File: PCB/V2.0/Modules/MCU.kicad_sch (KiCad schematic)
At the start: 4 parts, among them J13 Conn_02x04_Odd_Even, J15 Conn_02x04_Odd_Even, J28 Conn_02x20, J4 Conn_01x20

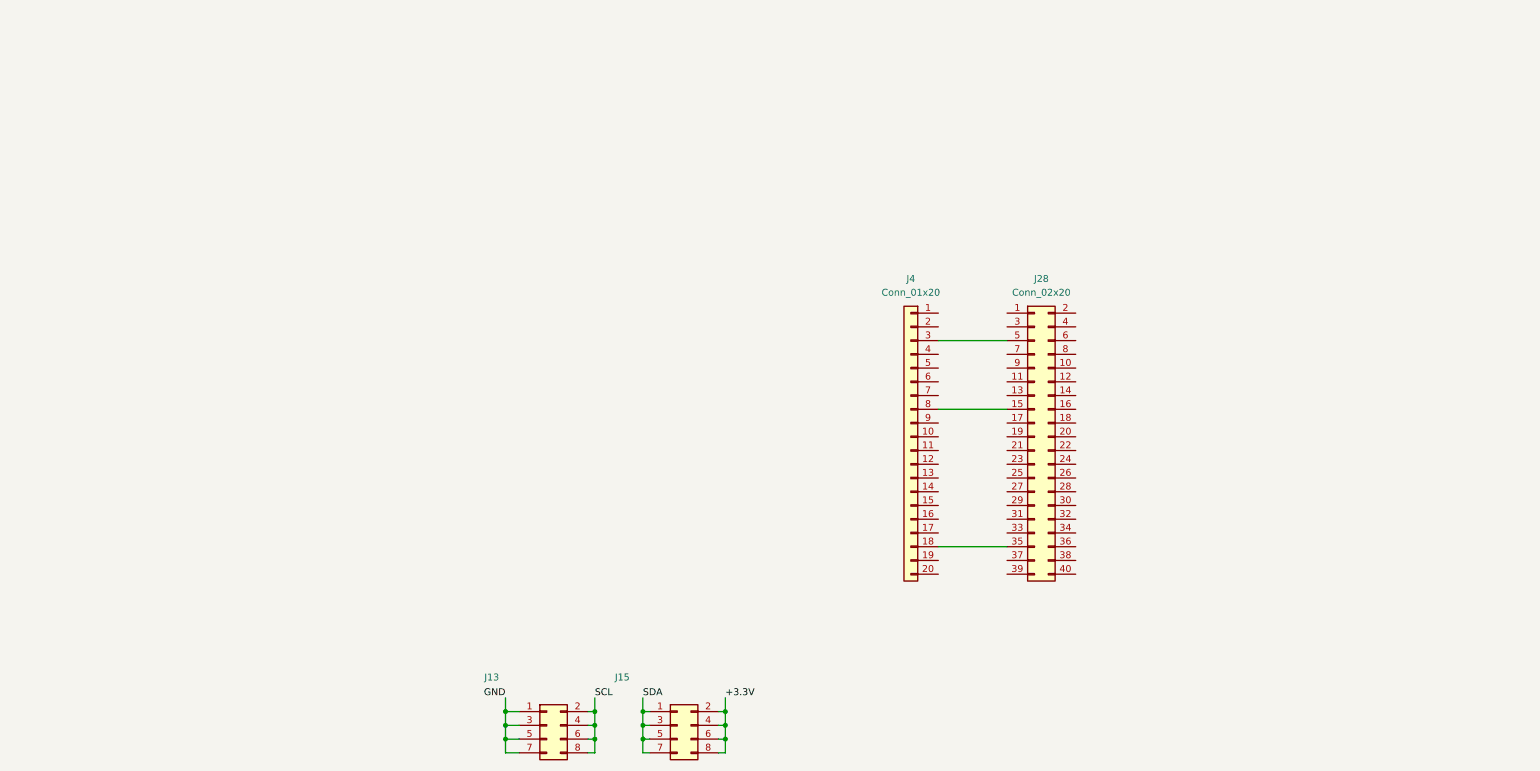
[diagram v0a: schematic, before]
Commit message: Update 2.0 - IMU and NRF24 support
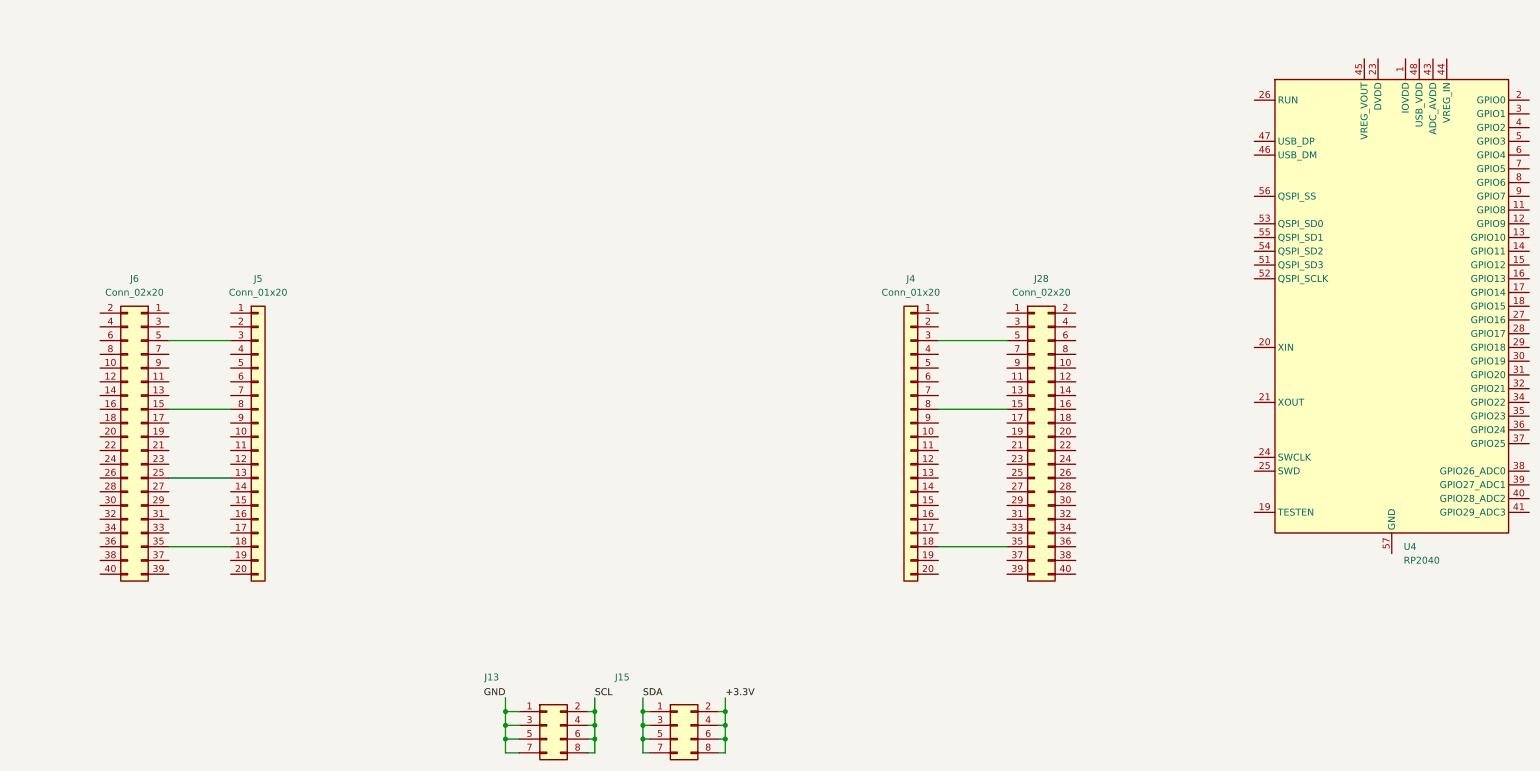
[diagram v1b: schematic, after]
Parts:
- added J5: Conn_01x20, Connector_PinSocket_2.54mm:PinSocket_1x20_P2.54mm_Vertical, symbol Connector_Generic:Conn_01x20
- added J6: Conn_02x20, Connector_PinHeader_2.54mm:PinHeader_2x20_P2.54mm_Vertical, symbol Connector_Generic:Conn_02x20_Odd_Even
- added U4: RP2040, Package_DFN_QFN:QFN-56-1EP_7x7mm_P0.4mm_EP3.2x3.2mm, symbol MCU_RaspberryPi:RP2040
- J4: footprint Connector_PinSocket_2.54mm:PinSocket_2x10_P2.54mm_Vertical -> Connector_PinSocket_2.54mm:PinSocket_1x20_P2.54mm_Vertical
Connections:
- new net: J5.13 (Pin_13), J6.25 (Pin_25)
- new net: J5.18 (Pin_18), J6.35 (Pin_35)
- new net: J5.3 (Pin_3), J6.5 (Pin_5)
- new net: J5.8 (Pin_8), J6.15 (Pin_15)
- new net: U4.1 (IOVDD), U4.10 (IOVDD), U4.22 (IOVDD), U4.33 (IOVDD), U4.42 (IOVDD), U4.49 (IOVDD)
- new net: U4.23 (DVDD), U4.50 (DVDD)

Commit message: Update V2.0 form factor
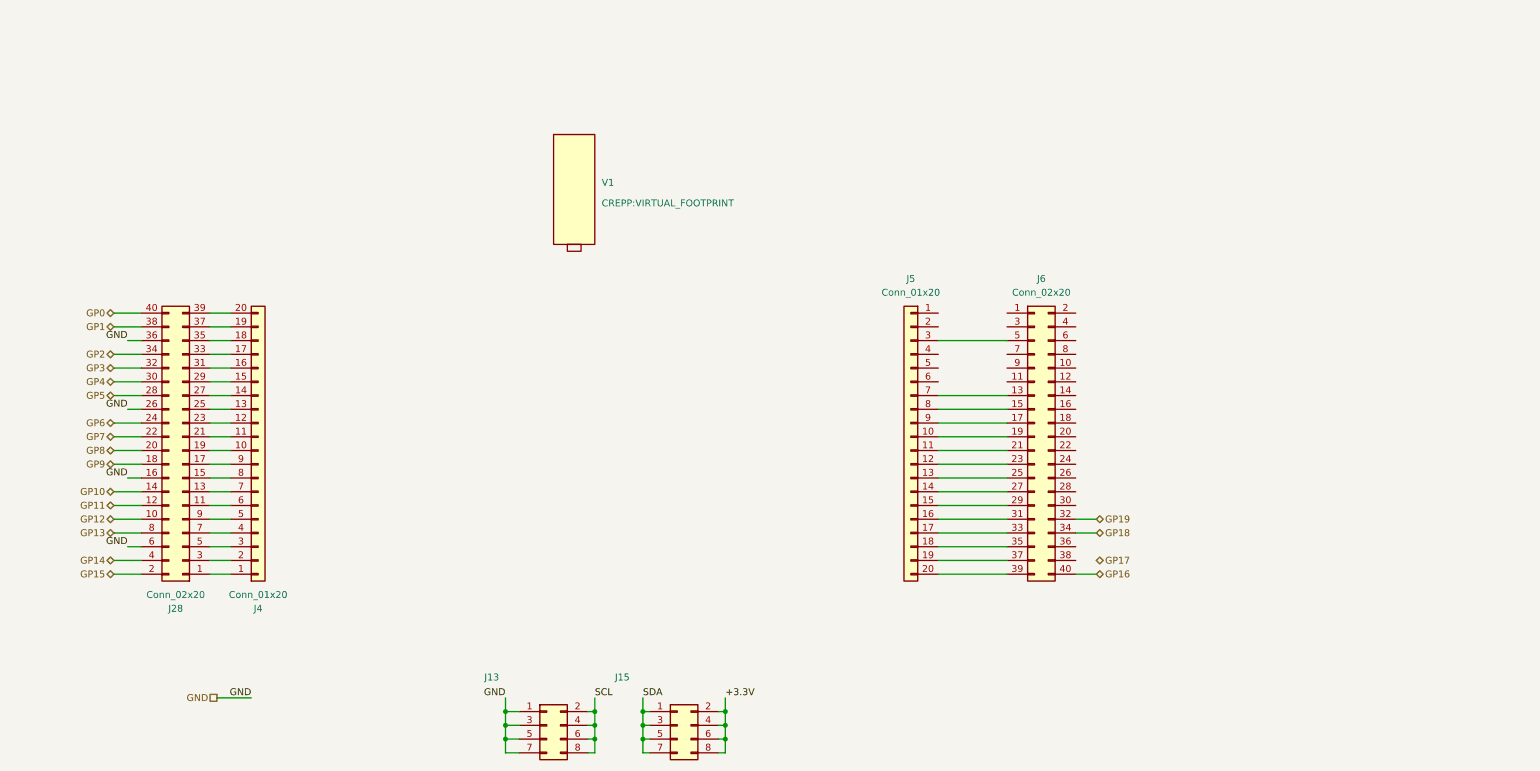
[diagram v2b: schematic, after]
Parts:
- removed U4: RP2040, Package_DFN_QFN:QFN-56-1EP_7x7mm_P0.4mm_EP3.2x3.2mm, symbol MCU_RaspberryPi:RP2040
- added V1: ~, CREPP:VIRTUAL_FOOTPRINT, symbol CREPP:RPI_PICO_VIRTUAL
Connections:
- net GND: now also J28.16 (Pin_16), J28.26 (Pin_26), J28.36 (Pin_36), J28.6 (Pin_6)
- net at J5.10 (Pin_10): now also J6.19 (Pin_19)
- net at J5.11 (Pin_11): now also J6.21 (Pin_21)
- net at J5.12 (Pin_12): now also J6.23 (Pin_23)
- net at J5.14 (Pin_14): now also J6.27 (Pin_27)
- net at J5.15 (Pin_15): now also J6.29 (Pin_29)
- net at J5.16 (Pin_16): now also J6.31 (Pin_31)
- net at J5.17 (Pin_17): now also J6.33 (Pin_33)
- net at J5.19 (Pin_19): now also J6.37 (Pin_37)
- net at J5.20 (Pin_20): now also J6.39 (Pin_39)
- net at J5.7 (Pin_7): now also J6.13 (Pin_13)
- net at J5.9 (Pin_9): now also J6.17 (Pin_17)
- net at J4.1 (Pin_1): now also J28.1 (Pin_1)
- net at J4.10 (Pin_10): now also J28.19 (Pin_19)
- net at J4.11 (Pin_11): now also J28.21 (Pin_21)
- net at J4.12 (Pin_12): now also J28.23 (Pin_23)
- net at J4.13 (Pin_13): now also J28.25 (Pin_25)
- net at J4.14 (Pin_14): now also J28.27 (Pin_27)
- net at J4.15 (Pin_15): now also J28.29 (Pin_29)
- net at J4.16 (Pin_16): now also J28.31 (Pin_31)
- net at J4.17 (Pin_17): now also J28.33 (Pin_33)
- net at J4.19 (Pin_19): now also J28.37 (Pin_37)
- net at J4.2 (Pin_2): now also J28.3 (Pin_3)
- net at J4.20 (Pin_20): now also J28.39 (Pin_39)
- net at J4.4 (Pin_4): now also J28.7 (Pin_7)
- net at J4.5 (Pin_5): now also J28.9 (Pin_9)
- net at J4.6 (Pin_6): now also J28.11 (Pin_11)
- net at J4.7 (Pin_7): now also J28.13 (Pin_13)
- net at J4.9 (Pin_9): now also J28.17 (Pin_17)
- net GP12: now reaches J28.10 (Pin_10)
- net GP11: now reaches J28.12 (Pin_12)
- net GP10: now reaches J28.14 (Pin_14)
- net GP9: now reaches J28.18 (Pin_18)
- net GP15: now reaches J28.2 (Pin_2)
- net GP8: now reaches J28.20 (Pin_20)
- net GP7: now reaches J28.22 (Pin_22)
- net GP6: now reaches J28.24 (Pin_24)
- net GP5: now reaches J28.28 (Pin_28)
- net GP4: now reaches J28.30 (Pin_30)
- net GP3: now reaches J28.32 (Pin_32)
- net GP2: now reaches J28.34 (Pin_34)
- net GP1: now reaches J28.38 (Pin_38)
- net GP14: now reaches J28.4 (Pin_4)
- net GP0: now reaches J28.40 (Pin_40)
- net GP13: now reaches J28.8 (Pin_8)
- net GP19: now reaches J6.32 (Pin_32)
- net GP18: now reaches J6.34 (Pin_34)
- net GP16: now reaches J6.40 (Pin_40)
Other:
- moved on the sheet: J28, J4, J5, J6

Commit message: Add img
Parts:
- added JP1, JP2, JP3: Jumper_2.54mm_red, CREPP_Jumpers:Jumper_2.54mm_red, symbol CREPP_Jumpers:Jumper_2.54mm_red
- added JP10, JP11, JP12, JP13, JP14, JP15, JP16, JP17, JP18, JP19, JP20, JP21, JP22, JP23, JP24, JP25, JP26, JP27, JP28, JP29, JP4, JP5, JP6, JP7, JP8, JP9: Jumper_2.54mm_green, CREPP_Jumpers:Jumper_2.54mm_green, symbol CREPP_Jumpers:Jumper_2.54mm_green
- added SERVO_SG1: ~, CREPP_Servo:SG90_Servo, symbol CREPP_Servomotors:Servomotor_SG90

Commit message: Update board
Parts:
- added SW9: SW_Left, Button_Switch_THT:SW_PUSH_6mm, symbol Switch:SW_Push
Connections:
- net GP4 is gone; now on net SDA: J28.30 (Pin_30)
- net GP5 is gone; now on net SCL: J28.28 (Pin_28)
- net +3.3V: now also J6.10 (Pin_10)
- net GND: now also J6.16 (Pin_16), J6.26 (Pin_26), J6.6 (Pin_6), SW9.2
- net at J5.1 (Pin_1): now also J6.1 (Pin_1)
- net RUN: now reaches J5.11 (Pin_11), J6.21 (Pin_21)
- net RUN: now also J6.22 (Pin_22), SW9.1
- net at J5.2 (Pin_2): now also J6.3 (Pin_3)
- net at J5.4 (Pin_4): now also J6.7 (Pin_7)
- net at J5.5 (Pin_5): now also J6.9 (Pin_9)
- net at J5.6 (Pin_6): now also J6.11 (Pin_11)
- net V_{BUS}: now reaches J6.2 (Pin_2)
- net GP22: now reaches J6.24 (Pin_24)
- net GP21: now reaches J6.28 (Pin_28)
- net GP20: now reaches J6.30 (Pin_30)
- net V_{SYS}: now reaches J6.4 (Pin_4)
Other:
- moved on the sheet: J13, J15, J28, J4, J5, J6, JP1, JP10, JP11, JP12, JP13, JP14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

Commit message: Update
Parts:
- removed JP8, JP9: Jumper_2.54mm_green, CREPP_Jumpers:Jumper_2.54mm_green, symbol CREPP_Jumpers:Jumper_2.54mm_green
- added JP8, JP9: Jumper_2.54mm_blue, CREPP_Jumpers:Jumper_2.54mm_blue, symbol CREPP_Jumpers:Jumper_2.54mm_blue
- SW9: value SW_Left -> SW_Reset
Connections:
- net GND: now also J6.36 (Pin_36)
- net GP17: now also J6.38 (Pin_38)
- net GP26: now also J6.20 (Pin_20)
- net GP27: now also J6.18 (Pin_18)
- net GP28: now also J6.14 (Pin_14)
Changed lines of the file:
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@@
 	(wire
 		(pts
+			(xy 247.65 118.11) (xy 251.46 118.11)
+		)
+		(stroke
+			(width 0)
+			(type default)
+		)
+	)
+	(wire
+		(pts
 			(xy 167.64 151.13) (xy 167.64 153.67)
 		)
@@
 	(wire
 		(pts
+			(xy 247.65 87.63) (xy 251.46 87.63)
+		)
+		(stroke
+			(width 0)
+			(type default)
+		)
+	)
+	(wire
+		(pts
 			(xy 87.63 105.41) (xy 91.44 105.41)
 		)
@@
 	(wire
 		(pts
+			(xy 247.65 115.57) (xy 251.46 115.57)
+		)
+		(stroke
+			(width 0)
+			(type default)
+		)
+	)
+	(wire
+		(pts
 			(xy 222.25 82.55) (xy 234.95 82.55)
 		)
@@
 	(wire
 		(pts
+			(xy 247.65 92.71) (xy 251.46 92.71)
+		)
+		(stroke
+			(width 0)
+			(type default)
+		)
+	)
+	(wire
+		(pts
 			(xy 247.65 113.03) (xy 251.46 113.03)
 		)
@@
 	(wire
 		(pts
+			(xy 247.65 95.25) (xy 251.46 95.25)
+		)
+		(stroke
+			(width 0)
+			(type default)
+		)
+	)
+	(wire
+		(pts
 			(xy 69.85 95.25) (xy 74.93 95.25)
 		)
@@
 	)
 	(label "GND"
+		(at 251.46 115.57 0)
+		(effects
+			(font
+				(size 1.27 1.27)
+			)
+			(justify left bottom)
+		)
+	)
+	(label "GND"
 		(at 251.46 77.47 0)
 		(effects
@@
 	(symbol
 		(lib_id "CREPP_Jumpers:Jumper_2.54mm_green")
-		(at 24.13 87.63 0)
-		(unit 1)
-		(exclude_from_sim yes)
-		(in_bom yes)
-		(on_board yes)
-		(dnp no)
-		(fields_autoplaced yes)
-		(property "Reference" "JP9"
-			(at 27.94 86.9949 0)
-			(effects
-				(font
-					(size 1.27 1.27)
-				)
-				(justify left)
-			)
-		)
-		(property "Value" "Jumper_2.54mm_green"
-			(at 24.13 89.916 0)
-			(effects
-				(font
-					(size 1.27 1.27)
-				)
-				(hide yes)
-			)
-		)
-		(property "Footprint" "CREPP_Jumpers:Jumper_2.54mm_green"
-			(at 24.13 87.63 0)
-			(effects
-				(font
-					(size 1.27 1.27)
-				)
-				(hide yes)
-			)
-		)
-		(property "Datasheet" "~"
-			(at 24.13 87.63 0)
-			(effects
-				(font
-					(size 1.27 1.27)
-				)
-				(hide yes)
-			)
-		)
-		(property "Description" "Jumper, 2-pole, open"
-			(at 24.13 87.63 0)
-			(effects
-				(font
-					(size 1.27 1.27)
-				)
-				(hide yes)
-			)
-		)
-		(instances
-			(project "CREPP.io"
-				(path "/8bcd0d00-b75f-4070-8d50-196a2022a31c/e5758719-e9ac-47cc-b357-8148e1c54986"
-					(reference "JP9")
-					(unit 1)
-				)
-			)
-		)
-	)
-	(symbol
-		(lib_id "CREPP_Jumpers:Jumper_2.54mm_green")
 		(at 262.89 113.03 0)
 		(unit 1)
@@
 			)
 		)
-		(property "Value" "SW_Left"
+		(property "Value" "SW_Reset"
 			(at 213.36 140.9699 90)
 			(effects
@@
 	(symbol
 		(lib_id "CREPP_Jumpers:Jumper_2.54mm_green")
-		(at 24.13 85.09 0)
-		(unit 1)
-		(exclude_from_sim yes)
-		(in_bom yes)
-		(on_board yes)
-		(dnp no)
-		(fields_autoplaced yes)
-		(property "Reference" "JP8"
-			(at 27.94 84.4549 0)
-			(effects
-				(font
-					(size 1.27 1.27)
-				)
-				(justify left)
-			)
-		)
-		(property "Value" "Jumper_2.54mm_green"
-			(at 24.13 87.376 0)
-			(effects
-				(font
-					(size 1.27 1.27)
-				)
-				(hide yes)
-			)
-		)
-		(property "Footprint" "CREPP_Jumpers:Jumper_2.54mm_green"
-			(at 24.13 85.09 0)
-			(effects
-				(font
-					(size 1.27 1.27)
-				)
-				(hide yes)
-			)
-		)
-		(property "Datasheet" "~"
-			(at 24.13 85.09 0)
-			(effects
-				(font
-					(size 1.27 1.27)
-				)
-				(hide yes)
-			)
-		)
-		(property "Description" "Jumper, 2-pole, open"
-			(at 24.13 85.09 0)
-			(effects
-				(font
-					(size 1.27 1.27)
-				)
-				(hide yes)
-			)
-		)
-		(instances
-			(project "CREPP.io"
-				(path "/8bcd0d00-b75f-4070-8d50-196a2022a31c/e5758719-e9ac-47cc-b357-8148e1c54986"
-					(reference "JP8")
-					(unit 1)
-				)
-			)
-		)
-	)
-	(symbol
-		(lib_id "CREPP_Jumpers:Jumper_2.54mm_green")
 		(at 53.34 72.39 0)
 		(unit 1)
@@
 	)
 	(symbol
+		(lib_id "CREPP_Jumpers:Jumper_2.54mm_blue")
+		(at 34.29 87.63 0)
+		(unit 1)
+		(exclude_from_sim yes)
+		(in_bom yes)
+		(on_board yes)
+		(dnp no)
+		(fields_autoplaced yes)
+		(property "Reference" "JP9"
+			(at 38.1 86.9949 0)
+			(effects
+				(font
+					(size 1.27 1.27)
+				)
+				(justify left)
+			)
+		)
+		(property "Value" "Jumper_2.54mm_blue"
+			(at 34.29 89.916 0)
+			(effects
+				(font
+					(size 1.27 1.27)
+				)
+				(hide yes)
+			)
+		)
+		(property "Footprint" "CREPP_Jumpers:Jumper_2.54mm_blue"
+			(at 34.29 87.63 0)
+			(effects
+				(font
+					(size 1.27 1.27)
+				)
+				(hide yes)
+			)
+		)
+		(property "Datasheet" "~"
+			(at 34.29 87.63 0)
+			(effects
+				(font
+					(size 1.27 1.27)
+				)
+				(hide yes)
+			)
+		)
+		(property "Description" "Jumper, 2-pole, open"
+			(at 34.29 87.63 0)
+			(effects
+				(font
+					(size 1.27 1.27)
+				)
+				(hide yes)
+			)
+		)
+		(instances
+			(project "CREPP.io"
+				(path "/8bcd0d00-b75f-4070-8d50-196a2022a31c/e5758719-e9ac-47cc-b357-8148e1c54986"
+					(reference "JP9")
+					(unit 1)
+				)
+			)
+		)
+	)
+	(symbol
 		(lib_id "Connector_Generic:Conn_02x20_Odd_Even")
 		(at 82.55 97.79 180)
@@
 					(unit 1)
 				)
+			)
+		)
+	)
+	(symbol
+		(lib_id "CREPP_Jumpers:Jumper_2.54mm_blue")
+		(at 34.29 85.09 0)
+		(unit 1)
+		(exclude_from_sim yes)
+		(in_bom yes)
+		(on_board yes)
+		(dnp no)
+		(fields_autoplaced yes)
+		(property "Reference" "JP8"
+			(at 38.1 84.4549 0)
+			(effects
+				(font
+					(size 1.27 1.27)
+				)
+				(justify left)
+			)
+		)
+		(property "Value" "Jumper_2.54mm_blue"
+			(at 34.29 87.376 0)
+			(effects
+				(font
+					(size 1.27 1.27)
+				)
+				(hide yes)
+			)
+		)
+		(property "Footprint" "CREPP_Jumpers:Jumper_2.54mm_blue"
+			(at 34.29 85.09 0)
+			(effects
+				(font
+					(size 1.27 1.27)
+				)
+				(hide yes)
+			)
+		)
+		(property "Datasheet" "~"
+			(at 34.29 85.09 0)
+			(effects
+				(font
+					(size 1.27 1.27)
+				)
+				(hide yes)
+			)
+		)
+		(property "Description" "Jumper, 2-pole, open"
+			(at 34.29 85.09 0)
+			(effects
+				(font
+					(size 1.27 1.27)
+				)
+				(hide yes)
+			)
+		)
+		(instances
+			(project ""
+				(path "/8bcd0d00-b75f-4070-8d50-196a2022a31c/e5758719-e9ac-47cc-b357-8148e1c54986"
+					(reference "JP8")
+					(unit 1)
+				)
